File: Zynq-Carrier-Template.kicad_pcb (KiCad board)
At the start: 2 copper layers, 49 x 41 mm, 8 parts, among them J1 Zynq_SoM, J3 USB_C_Receptacle_USB2.0_16P, U1 BQ25629RYKR

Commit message: Import JST_Pins and Inductor
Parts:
- removed REF**: IND_P3519R_API, 1uH_Inductor:IND_P3519R_API
- added J2: B2B-PH-K-S, JST_Pins:CONN2_B2B-PH-K-S_JST, F.Cu at (135.7, 103.6)
- added L1: L, Inductor_SMD:L_1008_2520Metric_Pad1.43x2.20mm_HandSolder, F.Cu at (138.9, 110.1)

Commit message: USB-C Schematic
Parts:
- added J4: Conn_01x03, Connector_PinHeader_2.54mm:PinHeader_1x03_P2.54mm_Vertical, F.Cu at (151.1, 118.2)
- added J5: Conn_01x03, Connector_PinHeader_2.54mm:PinHeader_1x03_P2.54mm_Vertical, F.Cu at (151.1, 101.4)
- added R1: 5.1k, Resistor_SMD:R_0603_1608Metric, F.Cu at (155.4, 117.1)
- added R2: 5.1k, Resistor_SMD:R_0603_1608Metric, F.Cu at (155.4, 119.6)
- added R3: 5.1k, Resistor_SMD:R_0603_1608Metric, F.Cu at (155.4, 122.1)
- added R4: 1M, Resistor_SMD:R_0603_1608Metric, F.Cu at (155.4, 124.6)
- added R5: 100k, Resistor_SMD:R_0603_1608Metric, F.Cu at (155.4, 100.4)
- added U12: SRV05-4, Package_TO_SOT_SMD:SOT-23-6, F.Cu at (151.4, 113.6)
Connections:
- net /VBUS renamed V_USB
- J1 pad 1: unconnected-(J1A-VIN-Pad1) -> +5V
- J1 pad 10: unconnected-(J1A-VIN-Pad10) -> +5V
- J1 pad 104: unconnected-(J1B-GND-Pad104) -> GND
- J1 pad 105: unconnected-(J1B-GND-Pad105) -> GND
- J1 pad 106: unconnected-(J1B-GND-Pad106) -> GND
- J1 pad 11: unconnected-(J1A-VIN-Pad11) -> +5V
- J1 pad 115: unconnected-(J1B-GND-Pad115) -> GND
- J1 pad 116: unconnected-(J1B-GND-Pad116) -> GND
- J1 pad 12: unconnected-(J1A-VIN-Pad12) -> +5V
- J1 pad 125: unconnected-(J1B-GND-Pad125) -> GND
- J1 pad 126: unconnected-(J1B-GND-Pad126) -> GND
- J1 pad 13: unconnected-(J1A-VIN-Pad13) -> +5V
- J1 pad 135: unconnected-(J1B-GND-Pad135) -> GND
- J1 pad 136: unconnected-(J1B-GND-Pad136) -> GND
- J1 pad 14: unconnected-(J1A-VIN-Pad14) -> +5V
- J1 pad 145: unconnected-(J1B-GND-Pad145) -> GND
- J1 pad 146: unconnected-(J1B-GND-Pad146) -> GND
- J1 pad 15: unconnected-(J1A-GND-Pad15) -> GND
- J1 pad 155: unconnected-(J1B-GND-Pad155) -> GND
- J1 pad 16: unconnected-(J1A-GND-Pad16) -> GND
- J1 pad 165: unconnected-(J1B-GND-Pad165) -> GND
- J1 pad 166: unconnected-(J1B-GND-Pad166) -> GND
- J1 pad 17: unconnected-(J1A-GND-Pad17) -> GND
- J1 pad 175: unconnected-(J1B-GND-Pad175) -> GND
- J1 pad 176: unconnected-(J1B-GND-Pad176) -> GND
- J1 pad 18: unconnected-(J1A-GND-Pad18) -> GND
- J1 pad 185: unconnected-(J1B-GND-Pad185) -> GND
- J1 pad 186: unconnected-(J1B-GND-Pad186) -> GND
- J1 pad 195: unconnected-(J1B-GND-Pad195) -> GND
- J1 pad 196: unconnected-(J1B-GND-Pad196) -> GND
- J1 pad 197: unconnected-(J1B-GND-Pad197) -> GND
- J1 pad 2: unconnected-(J1A-VIN-Pad2) -> +5V
- J1 pad 203: unconnected-(J1C-GND-Pad203) -> GND
- J1 pad 206: unconnected-(J1C-GND-Pad206) -> GND
- J1 pad 213: unconnected-(J1C-GND-Pad213) -> GND
- J1 pad 218: unconnected-(J1C-GND-Pad218) -> GND
- J1 pad 223: unconnected-(J1C-GND-Pad223) -> GND
- J1 pad 228: unconnected-(J1C-GND-Pad228) -> GND
- J1 pad 23: unconnected-(J1A-GND-Pad23) -> GND
- J1 pad 233: unconnected-(J1C-GND-Pad233) -> GND
- J1 pad 238: unconnected-(J1C-GND-Pad238) -> GND
- J1 pad 243: unconnected-(J1C-GND-Pad243) -> GND
- J1 pad 248: unconnected-(J1C-GND-Pad248) -> GND
- J1 pad 253: unconnected-(J1C-GND-Pad253) -> GND
- J1 pad 258: unconnected-(J1C-GND-Pad258) -> GND
- J1 pad 263: unconnected-(J1C-GND-Pad263) -> GND
- J1 pad 268: unconnected-(J1C-GND-Pad268) -> GND
- J1 pad 273: unconnected-(J1C-GND-Pad273) -> GND
- J1 pad 28: unconnected-(J1A-GND-Pad28) -> GND
- J1 pad 280: unconnected-(J1C-GND-Pad280) -> GND
- J1 pad 283: unconnected-(J1C-GND-Pad283) -> GND
- J1 pad 290: unconnected-(J1C-GND-Pad290) -> GND
- J1 pad 295: unconnected-(J1C-GND-Pad295) -> GND
- J1 pad 3: unconnected-(J1A-VIN-Pad3) -> +5V
- J1 pad 30: unconnected-(J1A-USB_D--Pad30) -> /USB_SOM_D-
- J1 pad 300: unconnected-(J1C-GND-Pad300) -> GND
- J1 pad 32: unconnected-(J1A-USB_D+-Pad32) -> /USB_SOM_D+
- J1 pad 39: unconnected-(J1A-GND-Pad39) -> GND
- J1 pad 4: unconnected-(J1A-VIN-Pad4) -> +5V
- J1 pad 44: unconnected-(J1A-GND-Pad44) -> GND
- J1 pad 5: unconnected-(J1A-VIN-Pad5) -> +5V
- J1 pad 51: unconnected-(J1A-GND-Pad51) -> GND
- J1 pad 6: unconnected-(J1A-VIN-Pad6) -> +5V
- J1 pad 62: unconnected-(J1A-GND-Pad62) -> GND
- J1 pad 63: unconnected-(J1A-GND-Pad63) -> GND
- J1 pad 7: unconnected-(J1A-VIN-Pad7) -> +5V
- J1 pad 72: unconnected-(J1A-GND-Pad72) -> GND
- J1 pad 75: unconnected-(J1A-GND-Pad75) -> GND
- J1 pad 8: unconnected-(J1A-VIN-Pad8) -> +5V
- J1 pad 81: unconnected-(J1A-GND-Pad81) -> GND
- J1 pad 82: unconnected-(J1A-GND-Pad82) -> GND
- J1 pad 87: unconnected-(J1A-GND-Pad87) -> GND
- J1 pad 9: unconnected-(J1A-VIN-Pad9) -> +5V
- J1 pad 96: unconnected-(J1A-GND-Pad96) -> GND
- J1 pad 99: unconnected-(J1A-GND-Pad99) -> GND
- J2 pad 1: unconnected-(J2-Pad1) -> GND
- J2 pad 2: unconnected-(J2-Pad2) -> VBAT
- J3 pad A5: unconnected-(J3-CC1-PadA5) -> Net-(J3-CC1)
- J3 pad A6: unconnected-(J3-D+-PadA6) -> /USB_D+
- J3 pad A7: unconnected-(J3-D--PadA7) -> /USB_D-
- J3 pad B5: unconnected-(J3-CC2-PadB5) -> Net-(J3-CC2)
- J3 pad B6: unconnected-(J3-D+-PadB6) -> /USB_D+
- J3 pad B7: unconnected-(J3-D--PadB7) -> /USB_D-
- J3 pad S1: unconnected-(J3-SHIELD-PadS1) -> Net-(J3-SHIELD)
- U1 pad 4: unconnected-(U1-D--Pad4) -> /USB_POW_D-
- U1 pad 5: unconnected-(U1-D+-Pad5) -> /USB_POW_D+

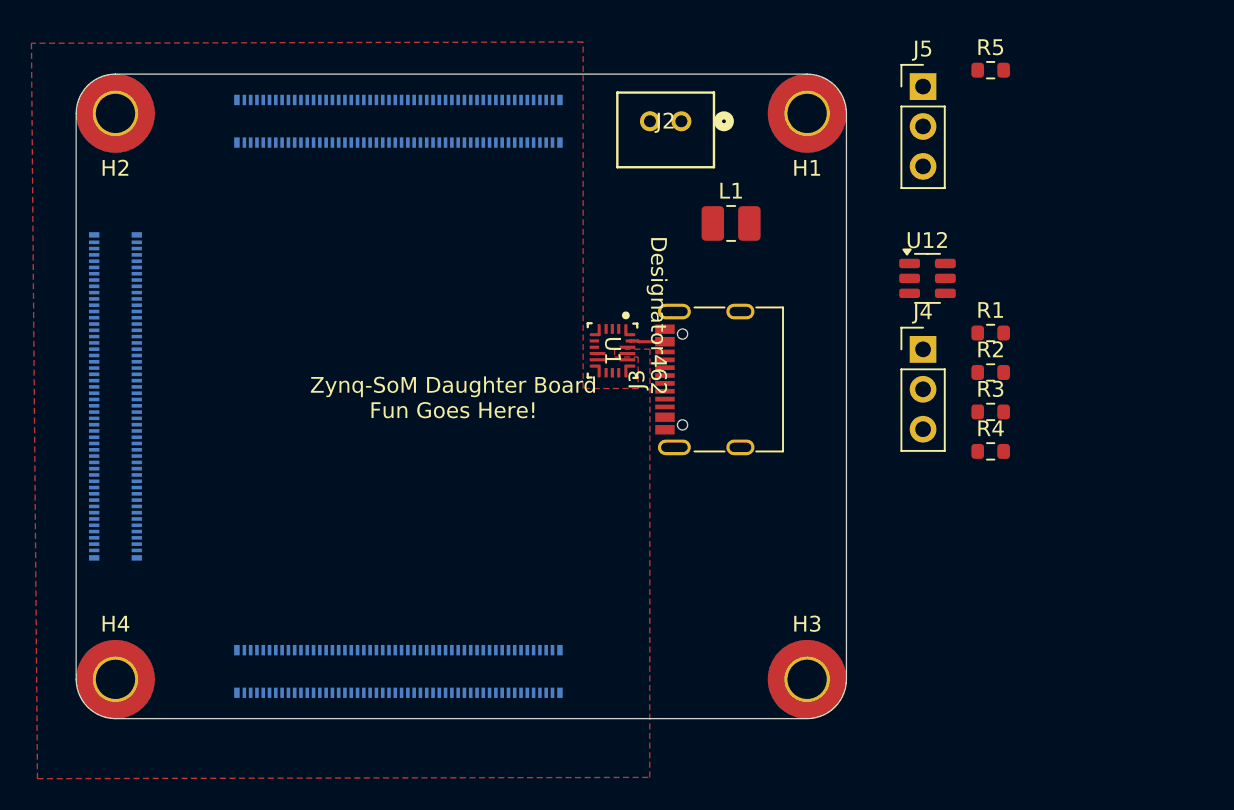
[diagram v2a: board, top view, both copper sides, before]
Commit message: Updated Schematic Switching Regulator Output
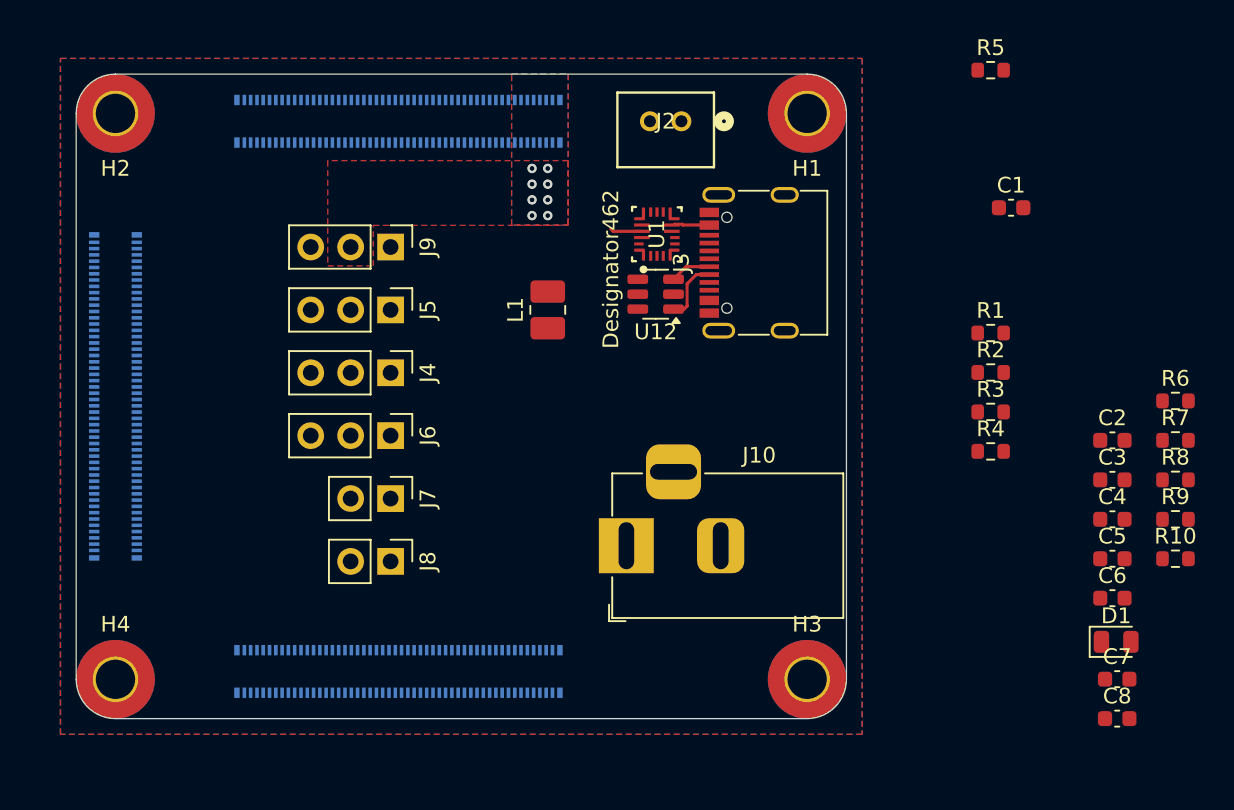
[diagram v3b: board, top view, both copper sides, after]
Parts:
- added C1: 10uf, Capacitor_SMD:C_0603_1608Metric, F.Cu at (156.7, 109.1)
- added C2: 0.1uf, Capacitor_SMD:C_0603_1608Metric, F.Cu at (163.1, 123.9)
- added C3: 10uf, Capacitor_SMD:C_0603_1608Metric, F.Cu at (163.1, 126.5)
- added C4: 0.1uf, Capacitor_SMD:C_0603_1608Metric, F.Cu at (163.1, 129.0)
- added C5: 10uf, Capacitor_SMD:C_0603_1608Metric, F.Cu at (163.1, 131.5)
- added C6: 0.1uf, Capacitor_SMD:C_0603_1608Metric, F.Cu at (163.1, 134.0)
- added C7: 4.7 uF, Capacitor_SMD:C_0603_1608Metric, F.Cu at (163.5, 139.1)
- added C8: 47 nF, Capacitor_SMD:C_0603_1608Metric, F.Cu at (163.5, 141.6)
- added D1: LED, LED_SMD:LED_0805_2012Metric, F.Cu at (163.4, 136.8)
- added J10: Barrel_Jack_MountingPin, Connector_BarrelJack:BarrelJack_Horizontal, F.Cu at (132.2, 130.6)
- added J6: Conn_01x03, Connector_PinHeader_2.54mm:PinHeader_1x03_P2.54mm_Vertical, F.Cu at (117.2, 123.6)
- added J7: Conn_01x02, Connector_PinHeader_2.54mm:PinHeader_1x02_P2.54mm_Vertical, F.Cu at (117.2, 127.6)
- added J8: Conn_01x02, Connector_PinHeader_2.54mm:PinHeader_1x02_P2.54mm_Vertical, F.Cu at (117.2, 131.6)
- added J9: Conn_01x03, Connector_PinHeader_2.54mm:PinHeader_1x03_P2.54mm_Vertical, F.Cu at (117.2, 111.6)
- added R10: 10K, Resistor_SMD:R_0603_1608Metric, F.Cu at (167.2, 131.5)
- added R6: 330, Resistor_SMD:R_0603_1608Metric, F.Cu at (167.2, 121.4)
- added R7: 10K, Resistor_SMD:R_0603_1608Metric, F.Cu at (167.2, 123.9)
- added R8: 4.7k, Resistor_SMD:R_0603_1608Metric, F.Cu at (167.2, 126.5)
- added R9: 4.7k, Resistor_SMD:R_0603_1608Metric, F.Cu at (167.2, 129.0)
- moved J5 36.7 mm to (117.2, 115.6), turned to -90 degrees
- moved J4 33.9 mm to (117.2, 119.6), turned to -90 degrees
- moved U12 17.3 mm to (134.1, 114.6), turned to 180 degrees
- moved L1 12.9 mm to (127.2, 115.6), turned to 90 degrees
- moved U1 7.94 mm to (134.2, 110.8), turned to 90 degrees
- moved J3 7.94 mm to (141.2, 112.6)
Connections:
- J4 pad 2: /USB_SOM_D- -> /USB_D-
- J5 pad 2: /USB_SOM_D+ -> /USB_D+
- L1 pad 1: unconnected-(L1-Pad1) -> Net-(U1-SW)
- L1 pad 2: unconnected-(L1-Pad2) -> VREG_OUT
- U1 pad 1: unconnected-(U1-BTST-Pad1) -> Net-(U1-BTST)
- U1 pad 10: unconnected-(U1-STAT-Pad10) -> Net-(U1-STAT)
- U1 pad 12: unconnected-(U1-SDA-Pad12) -> /SDA
- U1 pad 13: unconnected-(U1-SCL-Pad13) -> /SCL
- U1 pad 14: unconnected-(U1-CE_N-Pad14) -> /~{CSn}
- U1 pad 16: +5V -> Net-(U1-SW)
- U1 pad 17: unconnected-(U1-PMID-Pad17) -> Net-(U1-PMID)
- U1 pad 2: unconnected-(U1-REGN-Pad2) -> Net-(U1-REGN)
- U1 pad 6: unconnected-(U1-TS-Pad6) -> GND
- U1 pad 8: unconnected-(U1-BAT-Pad8) -> VBAT
- U1 pad 9: unconnected-(U1-SYS-Pad9) -> VREG_OUT
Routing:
- net /USB_D-: track 0.00 -> 4.01 mm
- net /USB_D+: track 0.00 -> 2.61 mm
- net Net-(U1-SW): track 0.00 -> 2.06 mm
- net +5V: vias 0 -> 8
- added copper zone on B.Cu, net +5V
- added copper zone on B.Cu, net GND
- added copper zone on F.Cu, net GND
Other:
- board text removed: "Zynq-SoM Daughter Board Fun Goes Here!"
